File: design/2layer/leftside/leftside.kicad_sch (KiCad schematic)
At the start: 192 parts, among them IC1 XCL240B333FR-G, IC2 XC9148G50CER-G, IC3 nRF52833-QDAA-R7, IC4 74AHCT125PW,118, IC5 MCP23018T-E_SS, J1 USB_C_Receptacle_USB2.0_16P, J2 Battery Pos, J3 Battery Neg, J4 OLED_128x32, J6 Conn_01x04, J7 F32Q-1A7H1-11012, U1 BQ27441-G1, U2 BQ24072RGT, U3 USB6B1, U5 PEC11L-4015F-S0015, U6 PEC11L-4015F-S0015, Y1 ECS-320-8-37B2-JTY-TR

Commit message: prepare to wire
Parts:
- removed C18: 1uF, ScottoKeebs_Components:Capacitor_0603, symbol Device:C_Small
- removed S26: CL-SA-12C4-22, SamacSys_Parts:CLSA12C422, symbol SamacSys_Parts:CL-SA-12C4-22
- added IC6: TPS22917DBVT, SOT95P280X145-6N, symbol SamacSys_Parts:TPS22917DBVT
- added LED1, LED2: White LED KW_EEL, KWEELP41RUS1U13K6L3X4X5R18, symbol SamacSys_Parts:KW_EELP41.RU-S1U1-3K6L-3X4X-5-R18
- added R11, R8: 270, Resistor_SMD:R_0603_1608Metric, symbol Device:R
- added R12: 100k, Resistor_SMD:R_0603_1608Metric, symbol Device:R
- added S25: CL-SA-12C4-22, SamacSys_Parts:CLSA12C422, symbol SamacSys_Parts:CL-SA-12C4-22
- C10: value 4.7uF -> 100pF
- J2: value Battery Pos -> Battery+
- J3: value Battery Neg -> Battery-
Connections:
- net 5V: now also IC4.1 (1~{OE}), IC4.10 (3~{OE}), IC4.13 (4~{OE})
- net BAT: now also U1.7 (SRN), U2.2 (BAT), U2.3 (BAT), U2.6 (EN1), R11.1, R8.1; no longer U1.8 (SRP)
- net CHG: now also LED1.1 (K)
- net GND: now also C25.1, C48.1, IC6.2 (GND), R12.1; no longer C10.2, C25.2, C48.2, IC4.1 (1~{OE}), IC4.10 (3~{OE}), IC4.13 (4~{OE})
- net OUT: now also C10.1, C48.2, IC6.1 (VIN), S25.2 (NO); no longer C48.1
- net VBUS: no longer U2.6 (EN1)
- net ~{PGOOD}: now also LED2.1 (K)
- net SRP: now reaches C17.1, J2.1 (Pin_1)
- net SRP: now also R6.2, U1.8 (SRP); no longer U2.2 (BAT), U2.3 (BAT)
- net at IC2.1 (BAT), IC2.3 (CE), L3.1: now also C25.2, IC6.5 (QOD), IC6.6 (VOUT); no longer C10.1, C25.1
- removed net BAT_SRN: R6.2, U1.7 (SRN)
- new net: IC6.3 (ON), R12.2, S25.1 (COM)
- new net: C10.2, IC6.4 (CT)
- new net: LED2.2 (A), R11.2
- new net: LED1.2 (A), R8.2
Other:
- note added: "Battery charging and USB power stage. Output 3.3V. ILIM set to 3k, calculated by 1550/x where x is input current limit. ISET set to 1.8k, calculated by 890/x where x is fast charge limit. x is set to 500mA to comply with USB standard. White LED for charging status with CHG. TPS2291 load switch for better stability when turning on/off. White LED for USB Power connection"
- note removed: "Battery charging and USB power stage. Output 3.3V. ILIM set to 3k, calculated by 1550/x where x is input current limit. ISET set to 1.8k, calculated by 890/x where x is fast charge limit. x is set to 500mA to comply with USB standard."
- moved on the sheet: C13, C17, C22, C23, C24, C26, C27, C47, C48, C7, F1, IC1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

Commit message: 5v led power plane added
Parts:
- removed C20: 100nF, ScottoKeebs_Components:Capacitor_0603, symbol Device:C_Small
- removed IC4: 74AHCT125PW,118, SamacSys_Parts:SOP65P640X110-14N, symbol SamacSys_Parts:74AHCT125PW,118
- removed IC5: MCP23018T-E_SS, SamacSys_Parts:SOP65P780X200-24N, symbol SamacSys_Parts:MCP23018T-E_SS
- added C18: 100nF, ScottoKeebs_Components:Capacitor_0603, symbol Device:C_Small
- added IC4: TCA9537DGSR, SOP50P490X110-10N, symbol SamacSys_Parts:TCA9537DGSR
- added IC7: SN74AHCT1G125DCKR, SOT65P210X110-5N, symbol SamacSys_Parts:SN74AHCT1G125DCKR
- added R13, R14: 4k7, Resistor_SMD:R_0603_1608Metric, symbol Device:R
- CHG1: renamed from CHG; footprint (none) -> TestPoint:TestPoint_Pad_D1.0mm
- IC6: value TPS22917DBVT -> TPS22917LDBVT
- R12: value 100k -> 10k
- ~{PGOOD}1: renamed from ~{PGOOD}; footprint (none) -> TestPoint:TestPoint_Pad_D1.0mm
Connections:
- net 3V3: now also R12.1, R9.1, C18.1, IC4.10 (VCC), R13.2, R14.2; no longer R9.2
- net 5V: now also IC7.5 (VCC)
- net CCW: now also IC3.16 (P0.18); no longer IC3.15 (P0.17)
- net CCW2: now also IC3.14 (P0.15); no longer IC3.16 (P0.18)
- net CHG: now also IC4.2 (P1)
- net CW: now also IC3.17 (P0.20); no longer IC3.14 (P0.15)
- net CW2: now also IC3.15 (P0.17); no longer IC3.17 (P0.20)
- net GND: now also C18.2, IC4.5 (GND), IC7.1 (~{OE}), IC7.3 (GND); no longer R12.1
- net GPOUT: now also R12.2, IC4.3 (P2)
- net INTA: now also IC4.7 (~{INT})
- net NO: now also IC4.4 (P3)
- net NO2: now also IC4.1 (P0)
- net OUT: now also S25.1 (COM); no longer S25.2 (NO)
- net SCL: now also IC4.8 (SCL), R13.1
- net SDA: now also IC4.9 (SDA), R14.1
- net at C14.1, IC3.29 (XC2): now also Y1.3 (OUT/IN); no longer Y1.1 (IN/OUT)
- net at C19.1, IC3.28 (XC1): now also Y1.1 (IN/OUT); no longer Y1.3 (OUT/IN)
- net at R10.1: now also IC7.4 (Y)
- net 2A renamed A
- net A: now also IC7.2 (A)
- new net: IC6.3 (ON), S25.2 (NO)
- new net: IC4.6 (~{RESET}), R9.2
- no-connect marks 32 -> 16
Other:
- note added: "Address: 0x49/73"
- note removed: "Address: 0b0100000 (0x20/32, last three bits set by voltage on addr pin)"
- moved on the sheet: C37, S25

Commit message: LS two layer complete
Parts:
- removed 5V_2, 5V_3, 5V_5, BAT_1, GND4: TestPoint, TestPoint:TestPoint_Pad_D1.5mm, symbol Connector:TestPoint
- removed C40, C46: 100nF, ScottoKeebs_Components:Capacitor_0603, symbol Device:C_Small
- added R15, R16: 22, Resistor_SMD:R_0603_1608Metric, symbol Device:R
- R3: value 3k -> 540
- R4: value 1k8 -> 590
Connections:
- net BAT: now also U2.5 (EN2); no longer U2.6 (EN1)
- net D+: now also R16.2; no longer IC3.13 (D+)
- net D-: now also R15.1; no longer IC3.12 (D-)
- net GND: now also U2.6 (EN1), U5.MH2; no longer U2.5 (EN2)
- net GPOUT: now also IC4.4 (P3); no longer IC4.3 (P2)
- net NO: now also IC4.3 (P2); no longer IC4.4 (P3)
- net Row 0: now also IC3.7 (P0.11); no longer IC3.4 (P0.04)
- net Row 1: now also IC3.6 (P1.09); no longer IC3.5 (P0.05)
- net Row 2: now also IC3.5 (P0.05); no longer IC3.6 (P1.09)
- net Row 3: now also IC3.4 (P0.04); no longer IC3.7 (P0.11)
- new net D2_N: IC3.12 (D-), R15.2
- new net D2_P: IC3.13 (D+), R16.1
- no-connect marks 16 -> 15
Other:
- note added: "Battery charging and USB power stage. Output 3.3V. ILIM controls input current limit calculated by 1550/R = limit. 3k = 500mA | 540 = 3A ISET controls battery current charge limit calculated by 890/R = limit. 1.8k = 500mA | 590 = 1.5A White LED for charging status with CHG. TPS2291 load switch for better stability when turning on/off. White LED for USB Power connection"
- note added: "GPIO Expander, EC11 Encoders, OLED and Cirque glidepoint trackpad"
- note removed: "Battery charging and USB power stage. Output 3.3V. ILIM set to 3k, calculated by 1550/x where x is input current limit. ISET set to 1.8k, calculated by 890/x where x is fast charge limit. x is set to 500mA to comply with USB standard. White LED for charging status with CHG. TPS2291 load switch for better stability when turning on/off. White LED for USB Power connection"
- note removed: "EC11 Encoders, OLED and Cirque glidepoint trackpad"
- note removed: "GPIO Expander"
- note removed: "Stitching Capacitors"
- moved on the sheet: 3V3_2, 3v3_1, 5V_1, 5V_4, ANT1, C1, C11, C12, C14, C15, C16, C18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

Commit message: place components for RS 2 layer
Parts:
- F1: value 600mA -> 6A
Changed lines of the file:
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@@
 			)
 		)
-		(property "Value" "600mA"
-			(at 180.594 68.326 90)
+		(property "Value" "6A"
+			(at 180.34 71.12 90)
 			(effects
 				(font

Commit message: prepare to add in EVQWGD001
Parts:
- removed C27: 10uF-lowESR, ScottoKeebs_Components:Capacitor_0603, symbol Device:C_Small
- removed IC2: XC9148G50CER-G, SamacSys_Parts:XC9147_8_USP-6C, symbol SamacSys_Parts:XC9148G50CER-G
- removed L3: 4.7uH, 1286ASH1R0MP2, symbol SamacSys_Parts:DFE201612E-4R7M=P2
- added IC5: XCL110A503KR-G, XCL103D503CRG, symbol SamacSys_Parts:XCL110A503KR-G
- added R17: 0, Resistor_SMD:R_0603_1608Metric, symbol Device:R
- C26: value 10uF-lowESR -> 10uF
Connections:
- net 5V: now also C26.2, IC5.6 (6/Vout); no longer C26.1
- net GND: now also C26.1, IC5.2 (2/AGND), IC5.4 (4/PGND), IC5.9 (9/EP); no longer C26.2
- net VBUS: now also R17.1; no longer C2.2, IC3.10 (VBUS)
- net at C25.2, IC6.5 (QOD), IC6.6 (VOUT): now also IC5.1 (1/VIN), IC5.3 (3/EN), IC5.7 (7/L1)
- new net: C2.2, IC3.10 (VBUS), R17.2
- new net: IC5.5 (5/Lx), IC5.8 (8/L2)
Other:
- moved on the sheet: C2, C25, C26

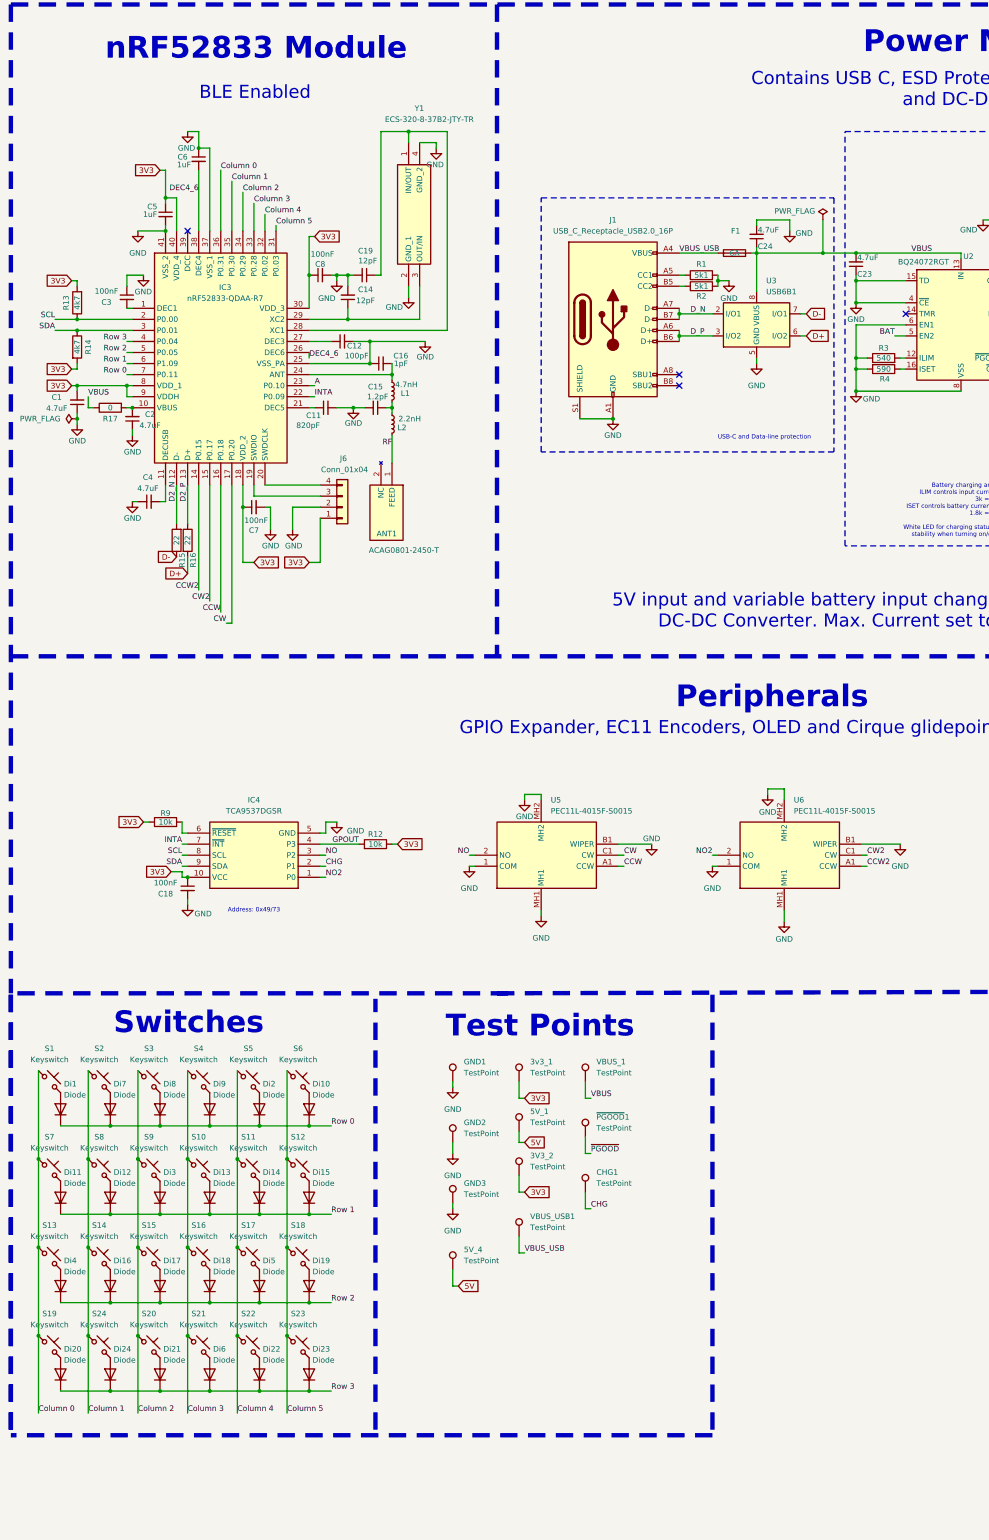
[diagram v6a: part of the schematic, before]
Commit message: begin better, more systematic 2 layer wiring
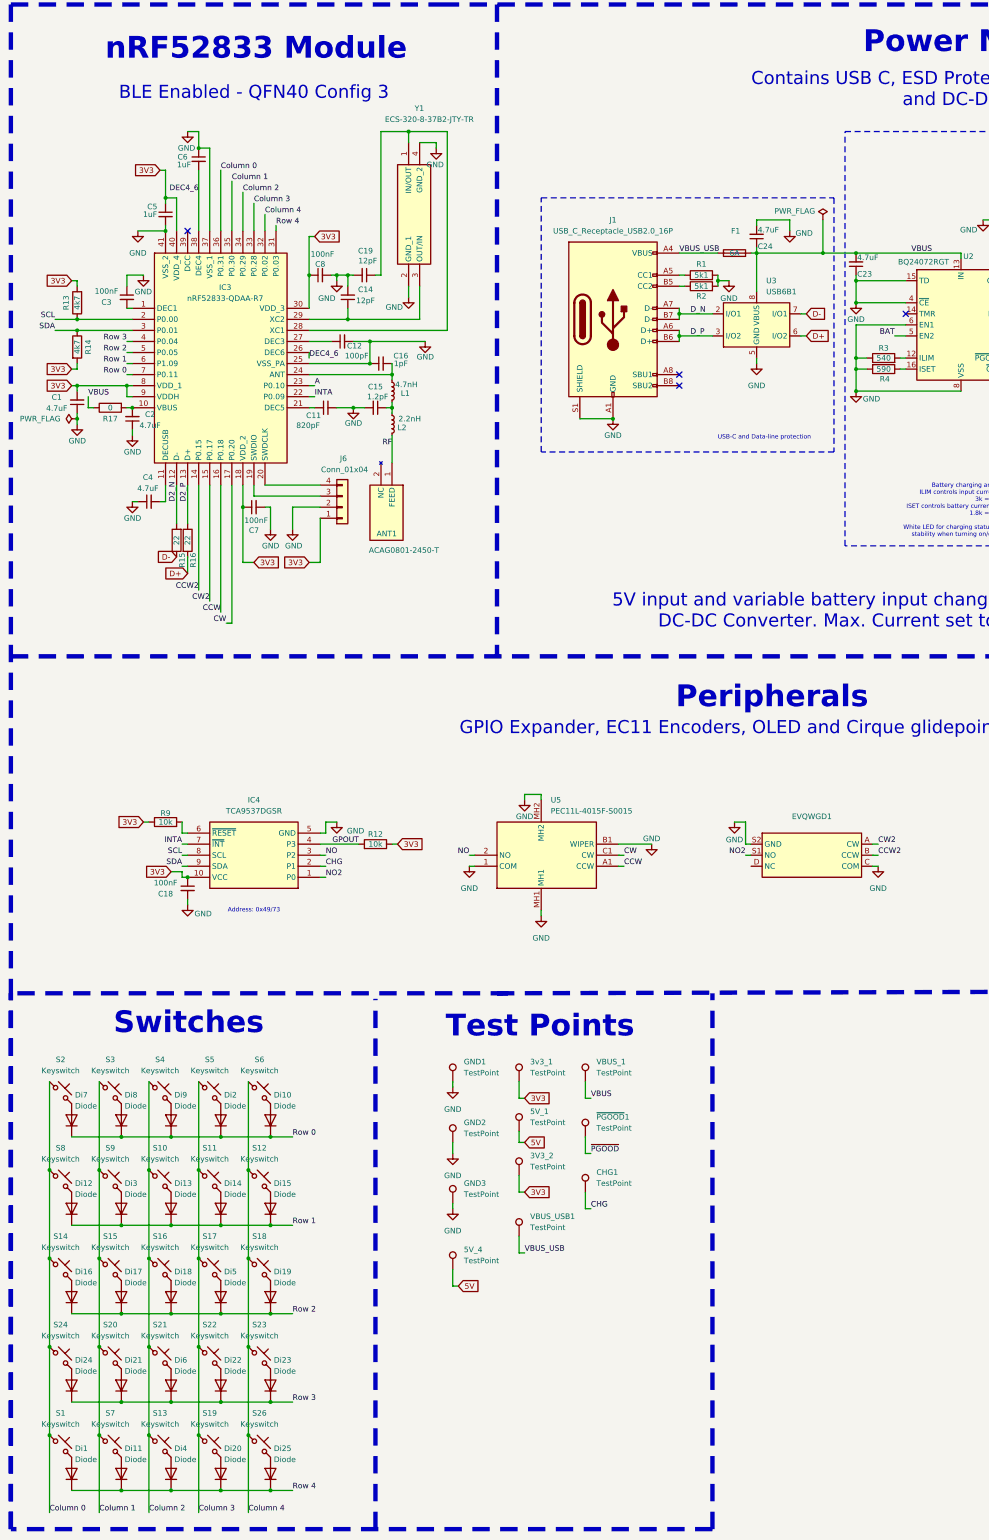
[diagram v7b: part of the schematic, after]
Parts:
- removed U6: PEC11L-4015F-S0015, SamacSys_Parts:PEC11L4015FS0015, symbol SamacSys_Parts:PEC11L-4015F-S0015
- added Di25: Diode, ScottoKeebs_Components:Diode_SOD-123, symbol ScottoKeebs:Placeholder_Diode
- added EVQWGD1: ~, SamacSys_Parts:RollerEncoder_Panasonic_EVQWGD001, symbol SamacSys_Parts:EVQWGD001
- added S26: Keyswitch, ScottoKeebs_Hotswap:Hotswap_Choc_V1V2_Plated_1.00u, symbol ScottoKeebs:Placeholder_Keyswitch
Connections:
- net CCW2: now also EVQWGD1.B (CCW)
- net CW2: now also EVQWGD1.A (CW)
- net Column 0: now also S14.1, S2.1, S24.1, S8.1; no longer S13.1, S19.1, S7.1
- net Column 1: now also S15.1, S20.1, S3.1, S7.1, S9.1; no longer S14.1, S2.1, S24.1, S8.1
- net Column 2: now also S10.1, S13.1, S16.1, S21.1, S4.1; no longer S15.1, S20.1, S3.1, S9.1
- net Column 3: now also S11.1, S17.1, S19.1, S22.1, S5.1; no longer S10.1, S16.1, S21.1, S4.1
- net Column 4: now also S12.1, S18.1, S23.1, S6.1, S26.1; no longer S11.1, S17.1, S22.1, S5.1
- net GND: now also EVQWGD1.C (COM), EVQWGD1.S2 (GND)
- net NO2: now also EVQWGD1.S1 (NO)
- net Row 0: no longer Di1.1 (K)
- net Row 1: no longer Di11.1 (K)
- net Row 2: no longer Di4.1 (K)
- net Row 3: no longer Di20.1 (K)
- removed net Column 5: IC3.31 (P0.03), S12.1, S18.1, S23.1, S6.1
- new net: Di25.2 (A), S26.2
- new net Row 4: Di1.1 (K), Di11.1 (K), Di20.1 (K), Di25.1 (K), Di4.1 (K), IC3.31 (P0.03)
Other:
- note added: "BLE Enabled - QFN40 Config 3"
- note removed: "BLE Enabled"
- moved on the sheet: Di1, Di10, Di11, Di12, Di13, Di14, Di16, Di17, Di18, Di19, Di2, Di20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

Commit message: V3 prep
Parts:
- removed IC1: XCL240B333FR-G, XCL103D503CRG, symbol SamacSys_Parts:XCL240B333FR-G
- removed IC4: TCA9537DGSR, SOP50P490X110-10N, symbol SamacSys_Parts:TCA9537DGSR
- removed R12: 10k, Resistor_SMD:R_0603_1608Metric, symbol Device:R
- added Di26, Di27, Di28, Di29, Di30, Di31, Di32, Di33, Di34, Di35, Di36: Diode, ScottoKeebs_Components:Diode_SOD-123, symbol ScottoKeebs:Placeholder_Diode
- added IC2: MCP23009-E_MG, QFN50P300X300X90-17N-D, symbol LibraryLoader:MCP23009-E_MG
- added IC8: TPS63051RMWT, QFN50P250X250X100-12N-D, symbol SamacSys:TPS63051RMWT
- added J5, J8: Conn_01x01, symbol Connector_Generic:Conn_01x01
- added PC1: 10uF, ScottoKeebs_Components:Capacitor_0603, symbol Device:C_Small
- added PC14: 47nF, ScottoKeebs_Components:Capacitor_0603, symbol Device:C_Small
- added PC2: 4.7uF, ScottoKeebs_Components:Capacitor_0603, symbol Device:C_Small
- added PG1: TestPoint, TestPoint:TestPoint_Pad_D1.5mm, symbol Connector:TestPoint
- added PL3: 10uH, Inductor_SMD:L_0603_1608Metric, symbol Device:L_Small
- added PL4: 15nH, Inductor_SMD:L_0603_1608Metric, symbol Device:L_Small
- added PL5: 1.5uH, Inductor_SMD:L_0603_1608Metric, symbol Device:L_Small
- added S27, S28, S29, S30, S31, S32, S33, S34, S35, S36, S37: Keyswitch, ScottoKeebs_Hotswap:Hotswap_Choc_V1V2_Plated_1.00u, symbol ScottoKeebs:Placeholder_Keyswitch
- added SR3: 10k, Resistor_SMD:R_0603_1608Metric, symbol Device:R
- added SR4: 4k7, Resistor_SMD:R_0603_1608Metric, symbol Device:R
- PC47: renamed from C47; value 4.7uF -> 10uF
- PR3: renamed from R3; value 540 -> 1k8
- PR4: renamed from R4; value 590 -> 1k
- SC10: renamed from C10; value 100pF -> 10nF
- renumbered C12 to PC10, C8 to PC11, C5 to PC12, C6 to PC13, C2 to PC16, C17 to PC17, C18 to PC18, C22 to PC22, C23 to PC23, C24 to PC24, C25 to PC25, C26 to PC26, C13 to PC27, C37 to PC37, C48 to PC48, C1 to PC6, C7 to PC7, C11 to PC8, C9 to PC9, R11 to PR11, R17 to PR17, R8 to PR8, C14 to SC1, C4 to SC19, C19 to SC2, C16 to SC3, C15 to SC4, C3 to SC5, L1 to SL1, L2 to SL2, R1 to SR1, R13 to SR13, R14 to SR14, R15 to SR15, R16 to SR16, R2 to SR2, R5 to SR5, R7 to SR7, R9 to SR9
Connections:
- net 3V3: now also IC2.3 (VDD), IC8.4 (VOUT), IC8.5 (FB), PC1.1, SR3.1
- net 5V: no longer PC47.1
- net BAT: now also PC2.1; no longer U1.6 (BAT)
- net CCW: now also IC3.15 (P0.17); no longer IC3.16 (P0.18)
- net CCW2: now also IC3.16 (P0.18); no longer IC3.14 (P0.15)
- net CHG: now also IC3.4 (P0.04)
- net CW: now also IC3.14 (P0.15); no longer IC3.17 (P0.20)
- net CW2: now also IC3.22 (P0.09); no longer IC3.15 (P0.17)
- net Column 0: now also S32.1
- net Column 1: now also S33.1
- net Column 2: now also S34.1
- net Column 3: now also S35.1
- net Column 4: now also S36.1
- net DEC4_6: now also PC14.1, PL4.2
- net GND: now also PC16.2, S25.1 (COM), IC2.1 (VSS), IC2.17 (EP), IC2.6 (ADDR), IC8.2 (GND_1), IC8.6 (PFM/PWM), IC8.9 (GND_2), J8.1 (Pin_1), PC1.2, PC14.2, PC2.2; no longer PC16.1
- net GPOUT: now also IC3.5 (P0.05)
- net INTA: now also IC3.23 (P0.10), IC2.8 (INT), SR3.2; no longer IC3.22 (P0.09)
- net NO: now also IC3.6 (P1.09)
- net NO2: now also IC3.7 (P0.11)
- net OUT: now also SR4.2; no longer S25.1 (COM)
- net Row 0: now also Di26.1 (K), IC2.9 (GP0); no longer IC3.7 (P0.11)
- net Row 1: now also Di27.1 (K), IC2.10 (GP1); no longer IC3.6 (P1.09)
- net Row 2: now also Di28.1 (K), IC2.11 (GP2); no longer IC3.5 (P0.05)
- net Row 3: now also Di29.1 (K), IC2.12 (GP3); no longer IC3.4 (P0.04)
- net Row 4: now also Di30.1 (K), IC2.13 (GP4); no longer IC3.31 (P0.03)
- net SCL: now also IC2.4 (SCL)
- net SDA: now also IC2.5 (SDA)
- net SRP: now also U1.6 (BAT)
- net at IC3.10 (VBUS), PR17.2: now also PC16.1; no longer PC16.2
- net at IC6.3 (ON), S25.2 (NO): now also SR4.1
- net at IC5.1 (1/VIN), IC5.3 (3/EN), IC5.7 (7/L1)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: now also PC47.1, IC8.10 (ILIM0), IC8.11 (EN), IC8.12 (VIN)
- net at SR5.2, U2.1 (TS): now also J5.1 (Pin_1)
- net at SR9.2: now also IC2.7 (~{RESET})
- net at IC3.39 (DCC): now also PL3.1
- net A renamed LED
- net LED: now also IC3.17 (P0.20); no longer IC3.23 (P0.10)
- new net: Di33.2 (A), S34.2
- new net: Di34.2 (A), S35.2
- new net: Di32.2 (A), S33.2
- new net: Di36.2 (A), S37.2
- new net: IC8.1 (L1), PL5.2
- new net: IC8.3 (L2), PL5.1
- new net: Di31.2 (A), S32.2
- new net: Di30.2 (A), S31.2
- new net: Di26.2 (A), S27.2
- new net: Di29.2 (A), S30.2
- new net: Di35.2 (A), S36.2
- new net: Di28.2 (A), S29.2
- new net: Di27.2 (A), S28.2
- new net: PL3.2, PL4.1
- new net Column 5: IC3.31 (P0.03), S27.1, S28.1, S29.1, S30.1, S31.1, S37.1
- new net PG: IC8.8 (PG), PG1.1
- new net Row 5: Di31.1 (K), Di32.1 (K), Di33.1 (K), Di34.1 (K), Di35.1 (K), Di36.1 (K), IC2.14 (GP5)
- no-connect marks 15 -> 18
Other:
- note added: "Address: 0x20/32"
- note added: "Battery charging and USB power stage. Output 3.3V. ILIM controls input current limit calculated by 1550/R = limit. 3k = 500mA | 1k8 = 860mA ISET controls battery current charge limit calculated by 890/R = limit. 1.8k = 500mA | 1k = 890mA White LED for charging status with CHG. TPS2291 load switch for better stability when turning on/off. White LED for USB Power connection Optional film NTC thermi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"
- note added: "USB-C and Data-line protection 5k1 resistor only guarantees 500mA"
- note removed: "Address: 0x49/73"
- note removed: "Battery charging and USB power stage. Output 3.3V. ILIM controls input current limit calculated by 1550/R = limit. 3k = 500mA | 540 = 3A ISET controls battery current charge limit calculated by 890/R = limit. 1.8k = 500mA | 590 = 1.5A White LED for charging status with CHG. TPS2291 load switch for better stability when turning on/off. White LED for USB Power connection"
- note removed: "USB-C and Data-line protection"
- moved on the sheet: IC5, PC13, PC16, PC18, PC25, PC26, PC27, PC47, PC48, SR5, SR9
